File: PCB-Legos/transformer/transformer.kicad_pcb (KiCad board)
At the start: 4 copper layers, 21.8 x 9.7 mm, 3 parts, among them J1 Conn_Coaxial, U1 NCS3-272+

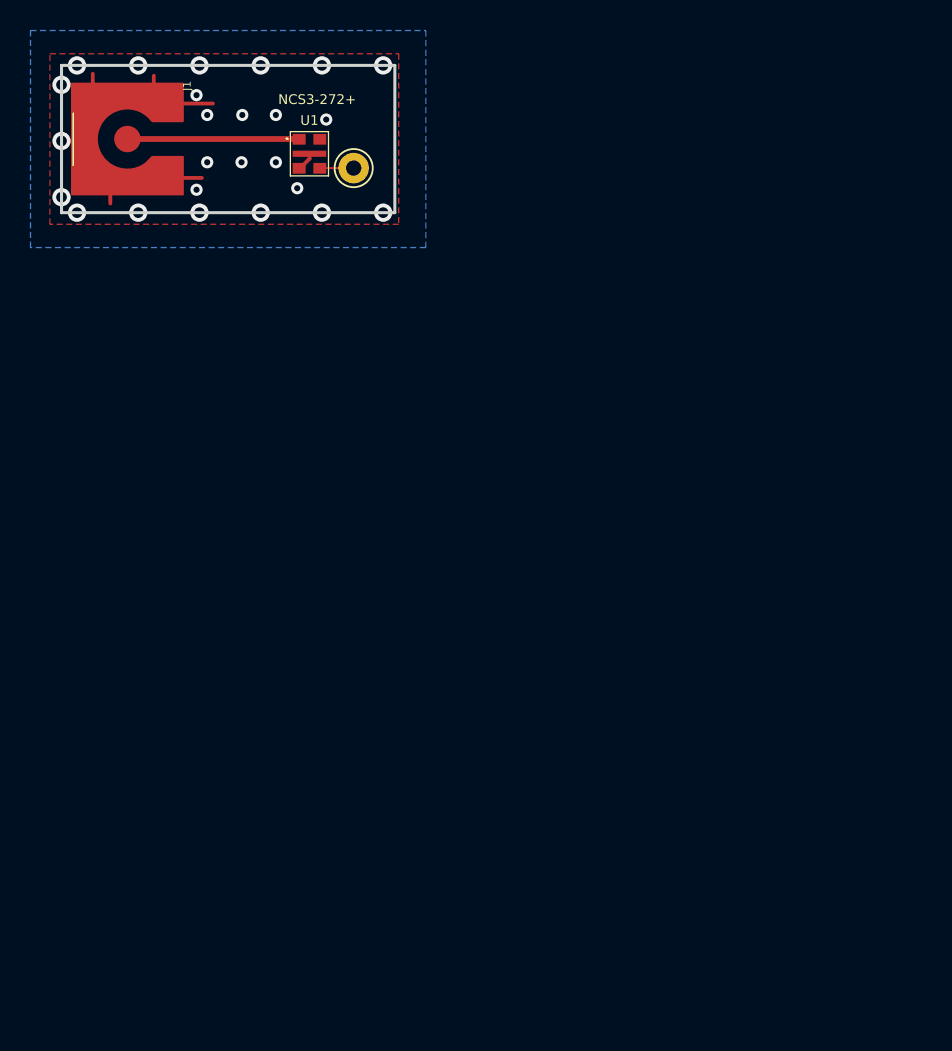
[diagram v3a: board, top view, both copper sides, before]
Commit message: Sent off for Fab, v1.0
Updated libraries and library paths; might actually not be terrible now with the submodule? Fixed footprint of transformer and rotated 90 degrees; made board OCD compliant and did via cleanup.
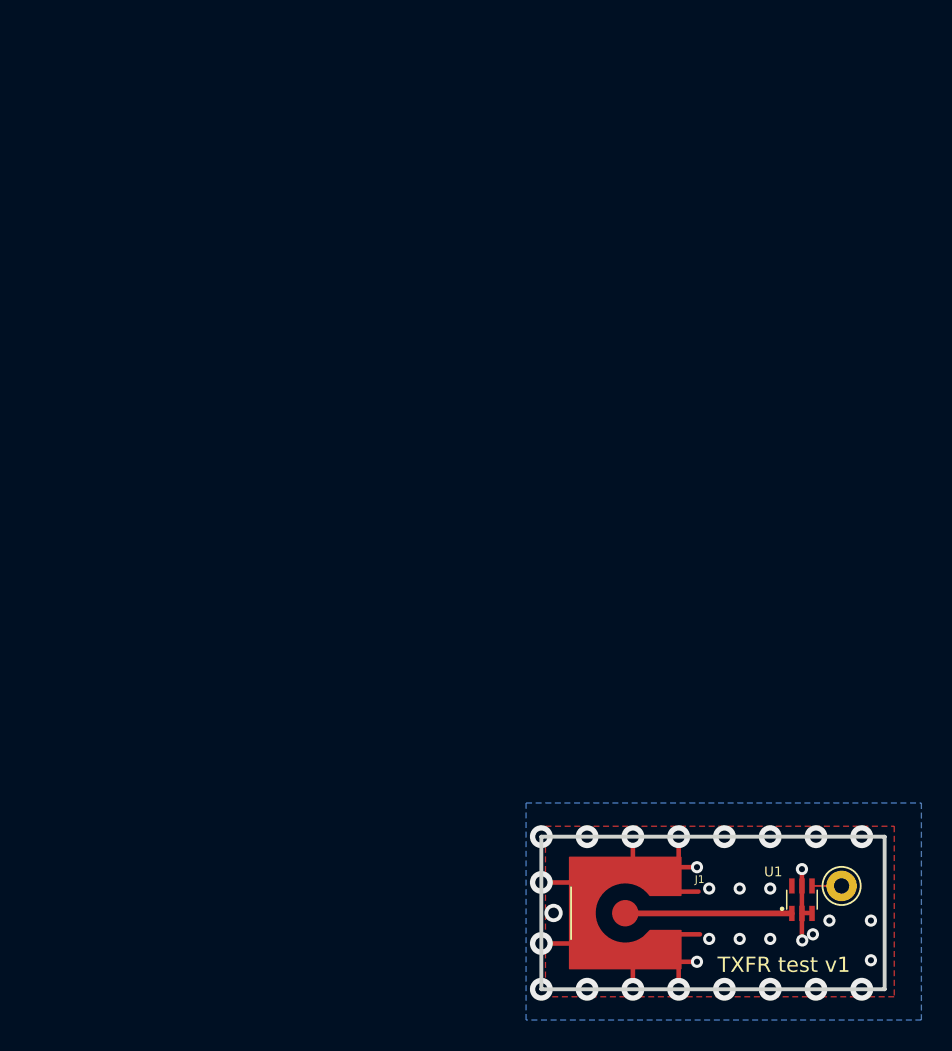
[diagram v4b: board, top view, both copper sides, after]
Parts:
- J1: footprint Footprints:J-Amphenol-132134-10-SMA-F-SMT-vertical -> footprints:J-Amphenol-132134-10-SMA-F-SMT-vertical
- U1: footprint NCS3-272+:FIL_MEM2012SC470 -> footprints:Minicircuits-GE0805C-9
- moved J1 60.3 mm to (135.5, 100.0)
- moved U1 58.6 mm to (147.1, 99.1), turned to 90 degrees
- moved H1 56.9 mm to (149.7, 98.2)
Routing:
- net GND: track 10.3 -> 24.9 mm, vias 25 -> 33
- net (no net): track 0.90 -> 0.00 mm
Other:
- board size 21.8 x 9.7 mm -> 22.5 x 10 mm
- board text added: "TXFR test v1"
